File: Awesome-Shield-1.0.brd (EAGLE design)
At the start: 51 x 55 mm, 21 parts, among them J1 PORT1, J2 PORT2, J3 PORT3, SW1 SPST_TACT-EVQQ2, SW2 DPDT, U1 LIGHTSENSORTEMT6000, X1 PASSER-07, X2 PASSER-07

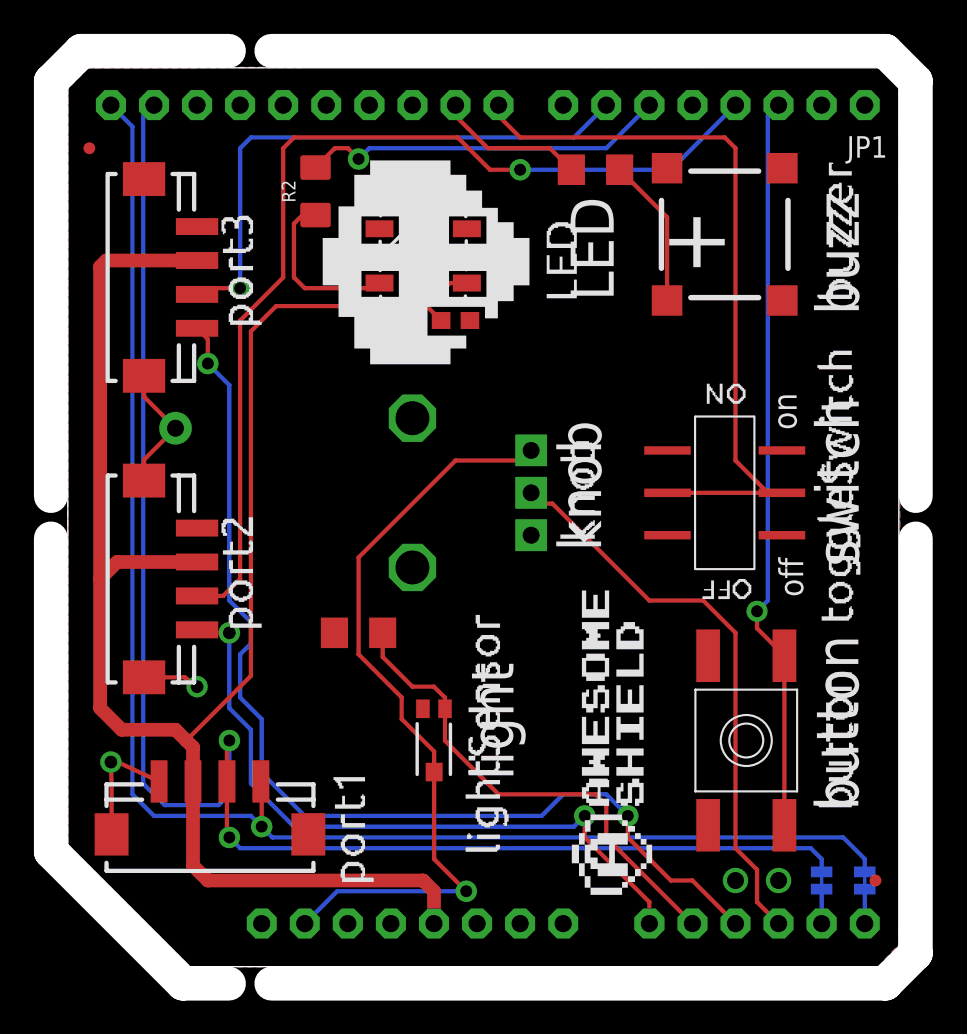
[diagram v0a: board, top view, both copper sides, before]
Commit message: add resistors to button, toggleSwitch, knob signal lines
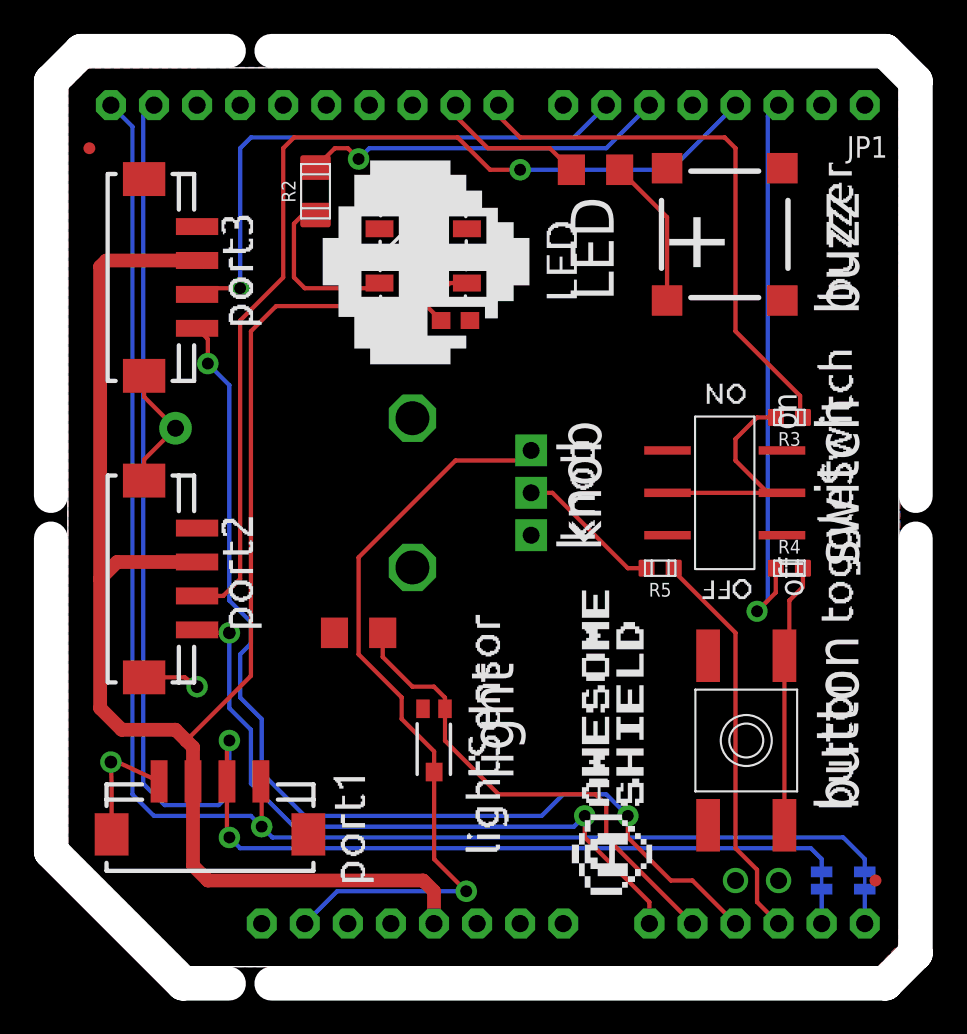
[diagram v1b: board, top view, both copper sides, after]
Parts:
- added R3, R4, R5: 1K, we-rcl:C0603
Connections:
- new net N$4: R3.1, SW2.2, SW2.5
- new net N$5: R5.1, RV1.P$2
- new net N$6: R4.1, SW1.B, SW1.B'
- net A3: now also R5.2; no longer RV1.P$2
- net D2: now also R4.2; no longer SW1.B, SW1.B'
- net D8: now also R3.2; no longer SW2.2, SW2.5
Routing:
- net N$6: track 0.00 -> 15.6 mm
- net N$4: track 0.00 -> 14.5 mm
- net D8: track 44.1 -> 32.9 mm
- net D2: track 43.7 -> 33.4 mm
- net A3: track 33.7 -> 23.5 mm
- net N$5: track 0.00 -> 8.65 mm
